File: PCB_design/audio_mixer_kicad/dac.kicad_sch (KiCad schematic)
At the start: 14 parts, among them U18 TAD5212IRGER

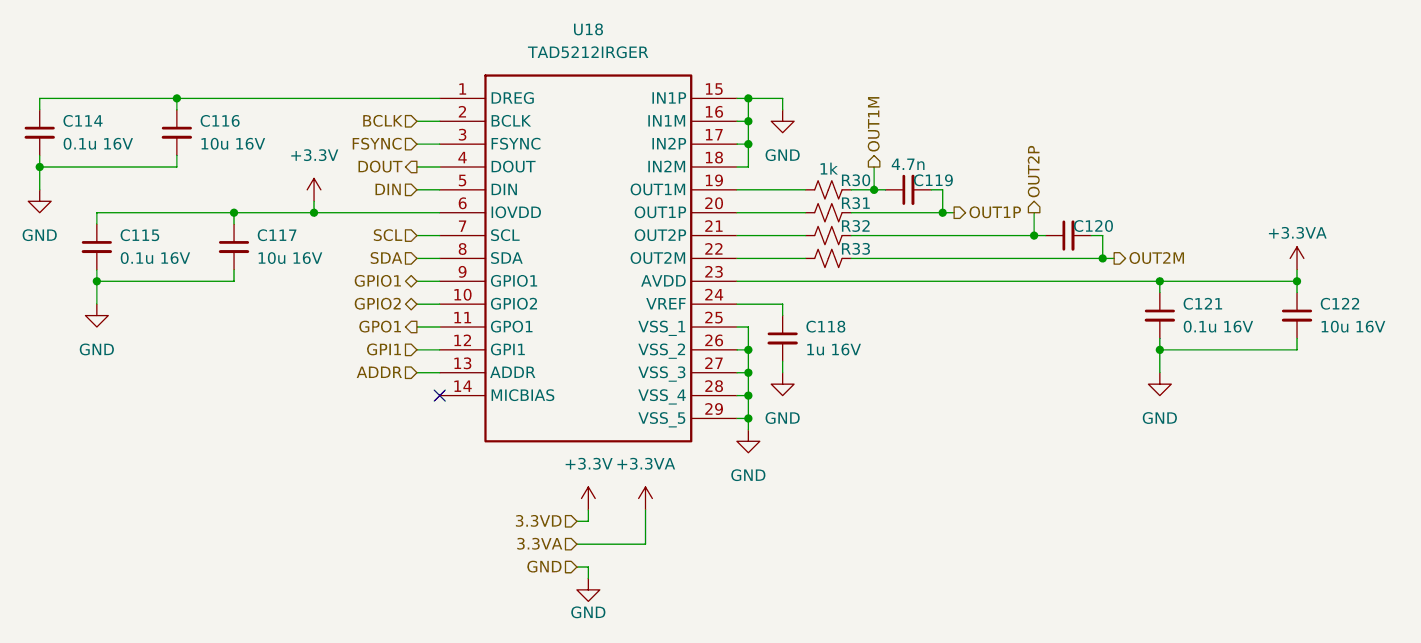
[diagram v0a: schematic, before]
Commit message: Reannotate and add passives for Y1
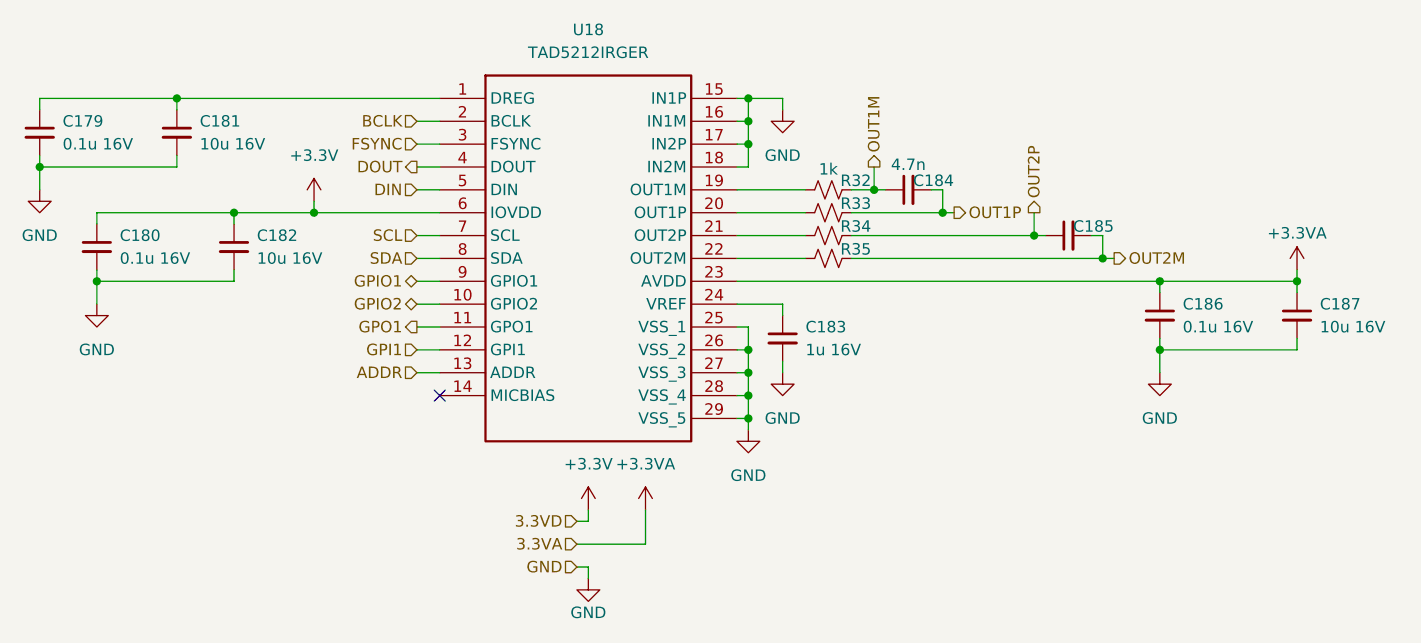
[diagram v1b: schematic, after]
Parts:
- renumbered C114 to C179, C115 to C180, C116 to C181, C117 to C182, C118 to C183, C119 to C184, C120 to C185, C121 to C186, C122 to C187, R30 to R32, R31 to R33, R32 to R34, R33 to R35
